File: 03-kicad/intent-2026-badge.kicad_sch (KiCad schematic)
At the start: 86 parts, among them J1 TYPE-C-16PIN, J2 HACK HEADER, J3 BATT 3xAAA, J4 PJ-320D, J5 IR, J6 AUDIO, J7 SPK, P1 IR MODULE, P2 AUDIO MODULE, P3 SPK MODULE, Q1 HL3401, Q2 S8050, SW1 BOOTSEL, SW2 A, SW3 B, SW4 C, SW5 MSK12C02, U1 RP2040, U2 W25Q16JVSNIQ, U3 ME6206A33M3G, U4 USBLC6-2SC6, U5 IRM-H638T/TR2, Y1 12MHz

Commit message: Rev 0.6: RP2040 design-guide review, SAO ports, re-layout, hand MCU re-route
Schematic/BOM (design.py, gen_sch.py):
- VREG decoupling per the RP2040 hardware design guide: 1 uF on VREG_VIN (C18)
  and VREG_VOUT (new C26), C10 100 nF on DVDD 50
- Y1 -> ABM8-272-T3 (C20625731), U3 -> AP2112K-3.3 (C51118) with 10 uF out,
  J1 -> HRO TYPE-C-31-M-12 (C165948), VBUS caps C27/C28, RESET button SW6
- RGB data buffer U6 SN74LV1T34 on VSYS (+C29)
- Expansion ports -> SAO 2x3 SMD sockets/headers, I2C0 on GPIO12/13 with
  4.7k pull-ups, GPIO2 on GPIO26-28; C22 now 0603
- ERC 0 errors / 0 warnings, netlist check 0 problems

PCB (placement.py, silk.py, art_copper.py, route2.py):
- RP2040 core re-placed after the guide (VREG caps and 27R next to the pins,
  QSPI_SS resistors at the flash), new parts placed, silk updated
- Router treats the exposed-copper art as a hard keepout
- Board as committed includes Benny's hand re-route of the MCU area in KiCad;
  build/routes.json and 04-fab are from the scripted route (BUILD-NOTES 16/17)

Also: review report (01-spec), BOM deltas EN/HE, GPIO map, Windows build
scripts (scripts/win), rev 0.5 fab outputs archived.

Co-Authored-By: Claude Opus 5.5 (1M context) <noreply@anthropic.com>
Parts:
- added C26, C27: 1uF, Capacitor_SMD:C_0402_1005Metric, symbol Device:C
- added C28, C29: 100nF, Capacitor_SMD:C_0402_1005Metric, symbol Device:C
- added R22, R23: 4.7k, Resistor_SMD:R_0402_1005Metric, symbol Device:R
- added SW6: RESET, Button_Switch_SMD:SW_Push_1P1T_XKB_TS-1187A, symbol Switch:SW_Push
- added U6: SN74LV1T34DBVR, Package_TO_SOT_SMD:SOT-23-5, symbol Logic_LevelTranslator:SN74LV1T34DBV
- C10: value 1uF -> 100nF; LCSC C6119792 -> C60474
- C18: value 100nF -> 1uF; LCSC C60474 -> C6119792
- C20: value 1uF -> 10uF; footprint Capacitor_SMD:C_0402_1005Metric -> Capacitor_SMD:C_0805_2012Metric; LCSC C6119792 -> C7503495
- C22: footprint Capacitor_SMD:C_0805_2012Metric -> Capacitor_SMD:C_0603_1608Metric; LCSC C7503495 -> C19702
- J1: value TYPE-C-16PIN -> TYPE-C-31-M-12; footprint intent:USB_C_TYPE-C16PIN_C393939 -> Connector_USB:USB_C_Receptacle_HRO_TYPE-C-31-M-12; LCSC C393939 -> C165948
- J5: value IR -> SAO1 IR; footprint Connector_PinSocket_2.54mm:PinSocket_1x03_P2.54mm_Vertical -> Connector_PinSocket_2.54mm:PinSocket_2x03_P2.54mm_Vertical_SMD; symbol Connector:Conn_01x03_Socket -> Connector_Generic:Conn_02x03_Odd_Even; LCSC C541850 -> C42163131
- J6: value AUDIO -> SAO2 AUDIO; footprint Connector_PinSocket_2.54mm:PinSocket_1x03_P2.54mm_Vertical -> Connector_PinSocket_2.54mm:PinSocket_2x03_P2.54mm_Vertical_SMD; symbol Connector:Conn_01x03_Socket -> Connector_Generic:Conn_02x03_Odd_Even; LCSC C541850 -> C42163131
- J7: value SPK -> SAO3 SPK; footprint Connector_PinSocket_2.54mm:PinSocket_1x03_P2.54mm_Vertical -> Connector_PinSocket_2.54mm:PinSocket_2x03_P2.54mm_Vertical_SMD; symbol Connector:Conn_01x03_Socket -> Connector_Generic:Conn_02x03_Odd_Even; LCSC C541850 -> C42163131
- P1, P2, P3: footprint Connector_PinHeader_2.54mm:PinHeader_1x03_P2.54mm_Vertical -> Connector_PinHeader_2.54mm:PinHeader_2x03_P2.54mm_Vertical_SMD; symbol Connector:Conn_01x03_Pin -> Connector_Generic:Conn_02x03_Odd_Even; LCSC C49257 -> C3294461
- U3: value ME6206A33M3G -> AP2112K-3.3TRG1; footprint Package_TO_SOT_SMD:SOT-23-3 -> Package_TO_SOT_SMD:SOT-23-5; symbol Regulator_Linear:XC6206PxxxMR -> Regulator_Linear:AP2112K-3.3; LCSC C35259 -> C51118
- Y1: value 12MHz -> 12MHz ABM8-272-T3; LCSC C133334 -> C20625731
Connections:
- net +1V1: now also C26.1
- net +3V3: now also J5.1 (Pin_1), J6.1 (Pin_1), J7.1 (Pin_1), U3.5 (VOUT), R22.2, R23.2; no longer J5.2 (Pin_2), J6.2 (Pin_2), J7.2 (Pin_2), U3.2 (VO)
- net AUDIO_PWM: now also J6.5 (Pin_5); no longer J6.3 (Pin_3)
- net AUM_GND: now also P2.2 (Pin_2); no longer P2.1 (Pin_1)
- net AUM_PWM: now also P2.5 (Pin_5); no longer P2.3 (Pin_3)
- net GND: now also J1.SH (SHIELD), J5.2 (Pin_2), J6.2 (Pin_2), J7.2 (Pin_2), U3.2 (GND), C26.2, C27.2, C28.2, C29.2, SW6.2, U6.3 (GND); no longer J1.S1 (SHIELD), J5.1 (Pin_1), J6.1 (Pin_1), J7.1 (Pin_1), U3.1 (GND)
- net IRM_3V3: now also P1.1 (Pin_1); no longer P1.2 (Pin_2)
- net IRM_GND: now also P1.2 (Pin_2); no longer P1.1 (Pin_1)
- net IRM_OUT: now also P1.5 (Pin_5); no longer P1.3 (Pin_3)
- net IR_OUT: now also J5.5 (Pin_5); no longer J5.3 (Pin_3)
- net RGB_DIN: now also U6.4 (Y); no longer U1.13 (GPIO10)
- net RUN: now also SW6.1
- net SPK_PWM: now also J7.5 (Pin_5); no longer J7.3 (Pin_3)
- net SPM_3V3: now also P3.1 (Pin_1); no longer P3.2 (Pin_2)
- net SPM_GND: now also P3.2 (Pin_2); no longer P3.1 (Pin_1)
- net SPM_SIG: now also P3.5 (Pin_5); no longer P3.3 (Pin_3)
- net VBUS: now also C27.1, C28.1
- net VSYS: now also U3.1 (VIN), C29.1, U6.5 (VCC)
- net GPIO12 renamed SAO_SDA
- net SAO_SDA: now also J5.3 (Pin_3), J6.3 (Pin_3), J7.3 (Pin_3), R22.1
- net GPIO13 renamed SAO_SCL
- net SAO_SCL: now also J5.4 (Pin_4), J6.4 (Pin_4), J7.4 (Pin_4), R23.1
- net GPIO26 renamed SAO1_GPIO2
- net SAO1_GPIO2: now also J5.6 (Pin_6)
- net GPIO27 renamed SAO2_GPIO2
- net SAO2_GPIO2: now also J6.6 (Pin_6)
- net GPIO28 renamed SAO3_GPIO2
- net SAO3_GPIO2: now also J7.6 (Pin_6)
- new net RGB_CTRL: U1.13 (GPIO10), U6.2 (A)
- no-connect marks 4 -> 15
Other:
- note added: "10 free GPIO + SAO I2C/GPIO2 + SPK_PWM + SWD + RUN + RGB out. TP1-TP3: UART0 115200 8N1. H1/H2: 4.0 mm lanyard holes."
- note added: "12/13 SAO I2C0; 26-28 SAO GPIO2 (ADC0-2); 29 VBUS sense;"
- note added: "14-21, 23/24 free on J2 (SPI1, UART1)."
- note added: "5-9 red LEDs; 10 WS2812 data (via U6); 11/22/25 SAO GPIO1;"
- note added: "C27/C28 VBUS decoupling. SBU pins unused."
- note added: "Crystal: Abracon ABM8-272-T3 (CL 10 pF, ESR 50 ohm) with 15 pF loads + 1k, exactly the RP2040 guide 2.3 circuit."
- note added: "Decoupling (RP2040 guide 2.1.2/2.1.3): 100 nF per IOVDD (6x), USB_VDD, ADC_AVDD, DVDD (C19 pin 23, C10 pin 50); 1 uF on VREG_VIN (C18) and VREG_VOUT (C26)."
- note added: "GPIO2: GPIO26/27/28 (ADC). Socket on badge, 2x3 pin header on the add-on."
- note added: "HRO TYPE-C-31-M-12 (C165948). 5.1k on CC1/CC2 = UFP."
- note added: "I2C0 on GPIO12/13, 4.7k pull-ups. GPIO1: IR 22 / AUDIO 11 / SPK 25."
- note added: "LED VDD spec is 3.7-5.3 V: firmware dims/stops the LEDs on low battery (VSYS < ~3.7 V). Chain out to J2 pin 19."
- note added: "P1: SAO 2x3 header, 1 = 3V3, 2 = GND, 5 = GPIO1 = OUT; plugs into J5. IRM_* nets live only on this board;"
- note added: "P2: SAO 2x3 header, 2 = GND, 5 = GPIO1 = PWM (3V3 unused); plugs into J6. Snap off; the jack then points sideways."
- note added: "P3: SAO 2x3, 1 = 3V3, 2 = GND, 5 = GPIO1 = SIG (J7)."
- note added: "RGB LEDs run from VSYS, everything else from 3V3 (AP2112K-3.3, 600 mA, EN tied to VIN)."
- note added: "SAO (badge.team): 1 3V3, 2 GND, 3 SDA, 4 SCL, 5 GPIO1, 6 GPIO2."
- note added: "SAO PORTS 3 x 2x3 socket"
- note added: "TESTEN tied to GND. RUN: 10k pull-up, SW6 RESET to GND, also on J2. BOOTSEL + tap RESET = UF2 mode."
- note added: "USBLC6-2 ESD array, 27R series (RP2040 guide)."
- note added: "WS2812B-2020-V6 x4 on VSYS, 100 nF each. GPIO10 -> U6 SN74LV1T34 (VCC = VSYS) -> DIN, so DIN swings to VSYS."
- note removed: "12-21, 23/24, 26-28 free on J2 (SPI1, I2C0, UART1, ADC0-2)."
- note removed: "15 free GPIO + SPK_PWM + SWD + RUN + RGB chain out. TP1-TP3: UART0 console 115200 8N1. H1/H2: 4.0 mm plated lanyard holes."
- note removed: "22 IR slot; 25 SPK slot (also J2.15); 29 VBUS sense (ADC3);"
- note removed: "5-9 red LEDs; 10 WS2812 data; 11 AUDIO slot (PWM);"
- note removed: "5.1k on CC1/CC2 = UFP (device). SBU pins unused."
- note removed: "Crystal 12 MHz: CL = 20 pF part with 15 pF loads (Pico values, ~ +50 ppm, fine for USB). R13 limits drive."
- note removed: "DIN is driven at 3.3 V against VIH = 0.7 x VDD: marginal on paper, works in practice."
- note removed: "Decoupling: one 100 nF per RP2040 supply pin (6x IOVDD, USB_VDD, ADC_AVDD, VREG_VIN); 1 uF + 100 nF on the 1V1 core rail."
- note removed: "EXPANSION PORTS 3 x 1x3 socket"
- note removed: "IR -> GPIO22, AUDIO -> GPIO11, SPK -> GPIO25 (also J2 pin 15)."
- note removed: "P1: 1 = GND, 2 = 3V3, 3 = OUT, mates with J5 (IR slot). IRM_* nets live only on this board;"
- note removed: "P2: 1 = GND, 2 = n.c. (no 3V3 needed), 3 = PWM, mates with J6 (AUDIO slot). Snap off; the jack then points sideways."
- note removed: "P3: 1 = GND, 2 = 3V3, 3 = SIG, mates with J7 (SPK slot)."
- note removed: "Power in the middle: a module plugged in backwards swaps GND"
- note removed: "RGB LEDs run from VSYS, everything else from 3V3 (ME6206, 300 mA)."
- note removed: "Same pinout on all three: 1 = GND (square pad), 2 = 3V3, 3 = signal."
- note removed: "TESTEN tied to GND. RUN has a 10k pull-up and is on J2 for an external reset / debugger."
- note removed: "USBLC6-2 ESD array in line, 27R series resistors"
- note removed: "WS2812B-2020-V6 x4 on VSYS (not 3V3), 100 nF each. Data from GPIO10, chain out to J2 pin 19."
- note removed: "and signal, never 3V3 onto a GPIO."
- note removed: "per the RP2040 hardware design guide."

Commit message: J3 -> JST B2B-PH-SM4-TB (C160352), drop SW5/JP1
- J3 battery-box plug is now a genuine JST PH 2-pin SMD vertical
  (C160352) on the stock KiCad footprint; pin 1 = BAT_IN, pin 2 = GND.
- SW5 and JP1 removed (Benny's schematic edit): J3 feeds Q1 directly.
  design.py, gen_sch.py, placement.py, silk.py synced to the KiCad
  schematic (check_sch: 313 pins, 78 nets, 0 problems).
- PCB: J3 footprint swapped in place, SW5/JP1 removed, JP1 pads bridged,
  SW5 stubs deleted. DRC 0 errors, 0 unconnected.
- 04-fab regenerated; BOM deltas (EN + HE), BUILD-NOTES item 19, CLAUDE.md.

Co-Authored-By: Claude Opus 5.5 (1M context) <noreply@anthropic.com>
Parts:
- removed JP1: SW5 bypass, Jumper:SolderJumper-2_P1.3mm_Bridged_Pad1.0x1.5mm, symbol Jumper:SolderJumper_2_Bridged
- removed SW5: MSK12C02, Button_Switch_SMD:SW_SPDT_Shouhan_MSK12C02, symbol Switch:SW_SPDT
- J3: footprint intent:JST_PH_2P_SMD_Vertical_C722761 -> Connector_JST:JST_PH_B2B-PH-SM4-TB_1x02-1MP_P2.00mm_Vertical; LCSC C722761 -> C160352
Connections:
- net BAT_SW is gone; now on net BAT_IN: Q1.3 (D)
- no-connect marks 15 -> 14

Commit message: IMU module replaces the audio module; module SAO headers rotated 90 deg
- B2 module: ST LSM6DS3TR-C (C967633) on the SAO I2C bus at 0x6A,
  INT1 -> GPIO11 (net IMU_INT1), INT2 -> GPIO27, 100 nF on VDD/VDDIO.
  Jack, PWM filter (J4, R17, C21, C22) removed; nets AUM_* -> IMM_*.
- Module headers P1-P3 at rot 90 like the badge sockets; speaker-can
  driver row moved to the back; module silk redrawn.
- PCB edits on the hand-routed board: only module copper re-routed;
  Benny's J3/BAT_IN edit kept. DRC 0 errors, 0 unconnected.
- 04-fab regenerated; BOM deltas EN/HE, BUILD-NOTES 20/21, GPIO map.

Co-Authored-By: Claude Opus 5.5 (1M context) <noreply@anthropic.com>
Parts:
- removed C21: 10nF, Capacitor_SMD:C_0402_1005Metric, symbol Device:C
- removed C22: 10uF, Capacitor_SMD:C_0603_1608Metric, symbol Device:C
- removed J4: PJ-320D, intent:Jack_3.5mm_PJ-320D_SMD_C431535, symbol Connector_Audio:AudioJack4
- removed R17: 1k, Resistor_SMD:R_0402_1005Metric, symbol Device:R
- added C30, C31: 100nF, Capacitor_SMD:C_0402_1005Metric, symbol Device:C
- added U7: LSM6DS3TR-C, Package_LGA:LGA-14_3x2.5mm_P0.5mm_LayoutBorder3x4y, symbol Sensor_Motion:LSM6DS3
- J6: value SAO2 AUDIO -> SAO2 IMU
- P2: value AUDIO MODULE -> IMU MODULE
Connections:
- net IMM_3V3: now reaches P2.1 (Pin_1)
- net IMM_3V3: now also C30.1, C31.1, U7.12 (CS), U7.5 (VDDIO), U7.8 (VDD)
- net IMM_SDA: now reaches P2.3 (Pin_3)
- net IMM_SDA: now also U7.14 (SDA)
- net IMM_SCL: now reaches P2.4 (Pin_4)
- net IMM_SCL: now also U7.13 (SCL)
- net IMM_INT2: now reaches P2.6 (Pin_6)
- net IMM_INT2: now also U7.9 (INT2)
- net AUDIO_PWM renamed IMU_INT1
- net AUM_GND renamed IMM_GND
- net IMM_GND: now also C30.2, C31.2, U7.1 (SDO/SA0), U7.2 (SDX), U7.3 (SCX), U7.6 (GND), U7.7 (GND)
- net AUM_PWM renamed IMM_INT1
- net IMM_INT1: now also U7.4 (INT1)
- no-connect marks 14 -> 12
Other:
- note added: "I2C0 on GPIO12/13, 4.7k pull-ups. GPIO1: IR 22 / IMU 11 / SPK 25."
- note added: "IMU MODULE breakaway board, plugs into J6"
- note added: "J3: JST B2B-PH-SM4-TB (C160352) for the 3xAAA box; the power switch is on the box."
- note added: "P2: SAO 2x3, 1 3V3, 2 GND, 3 SDA, 4 SCL, 5 GPIO1 = INT1 (GPIO11), 6 GPIO2 = INT2 (GPIO27). Plugs into J6."
- note added: "SDx/SCx = GND, pins 10/11 NC. 100 nF on VDD (C30) and VDDIO (C31). I2C pull-ups are on the badge (R22/R23)."
- note added: "ST LSM6DS3TR-C 6-axis IMU (C967633), I2C mode (datasheet Mode 1): CS = VDDIO, SA0 = GND -> 0x6A,"
- note removed: "AUDIO MODULE breakaway board, plugs into J6"
- note removed: "GPIO11 PWM (>= 100 kHz carrier) -> 1k / 10n low-pass (fc ~ 16 kHz) -> 10 uF DC block -> tip + ring 1 (mono). Sleeve + ring 2 = GND."
- note removed: "I2C0 on GPIO12/13, 4.7k pull-ups. GPIO1: IR 22 / AUDIO 11 / SPK 25."
- note removed: "Level into 32 ohm ~ 0.1 Vpp. PJ-320D (C431535) SMD pads: 1 = S, 2 = R2, 3 = R1, 4 = T. Detect-switch pads unused."
- note removed: "P2: SAO 2x3 header, 2 = GND, 5 = GPIO1 = PWM (3V3 unused); plugs into J6. Snap off; the jack then points sideways."
- note removed: "SW5 is DNP (the switch is on the battery box); JP1 bridges it. Cut JP1 only if SW5 is fitted."
- moved on the sheet: P2

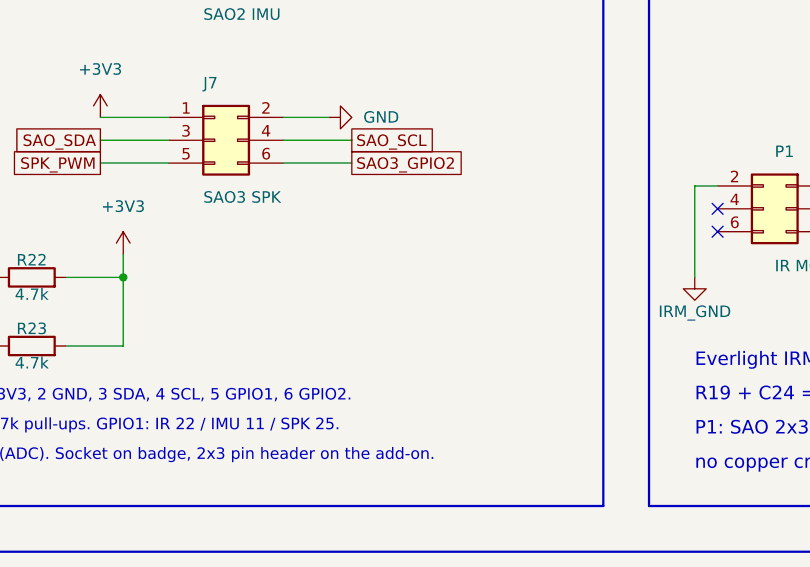
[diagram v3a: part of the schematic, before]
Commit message: Add J8, 4-pin I2C socket for a 0.96" OLED module
- J8: 1x4 2.54 mm SMD female socket (C42379197), 1 GND, 2 3V3, 3 SCL,
  4 SDA on the SAO I2C bus; placed by Benny under the logo.
- Routed locally to the existing +3V3 / SAO_SCL / SAO_SDA copper.
  DRC 0 errors, 0 unconnected. 04-fab regenerated; BOM deltas EN/HE,
  BUILD-NOTES item 22.

Co-Authored-By: Claude Opus 5.5 (1M context) <noreply@anthropic.com>
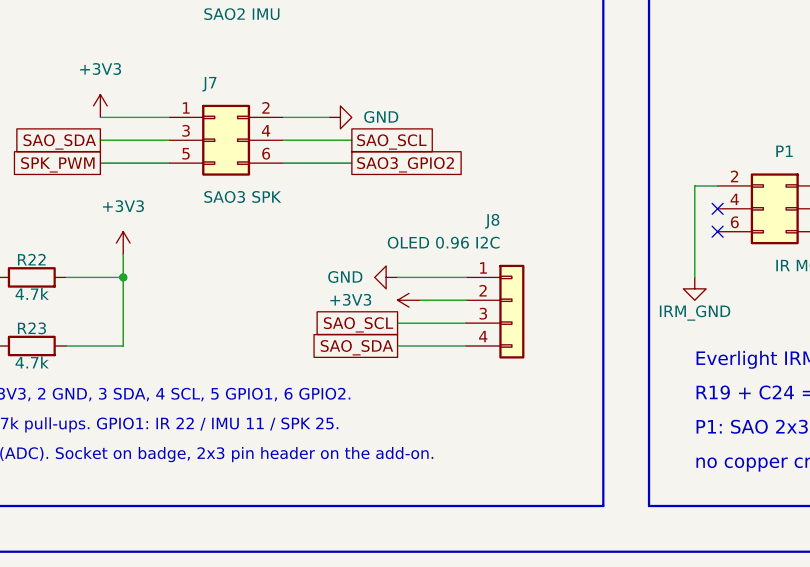
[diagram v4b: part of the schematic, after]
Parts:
- added J8: OLED 0.96 I2C, Connector_PinSocket_2.54mm:PinSocket_1x04_P2.54mm_Vertical_SMD_Pin1Right, symbol Connector_Generic:Conn_01x04
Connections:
- net +3V3: now also J8.2 (Pin_2)
- net GND: now also J8.1 (Pin_1)
- net SAO_SCL: now also J8.3 (Pin_3)
- net SAO_SDA: now also J8.4 (Pin_4)
